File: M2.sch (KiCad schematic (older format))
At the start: 3 parts

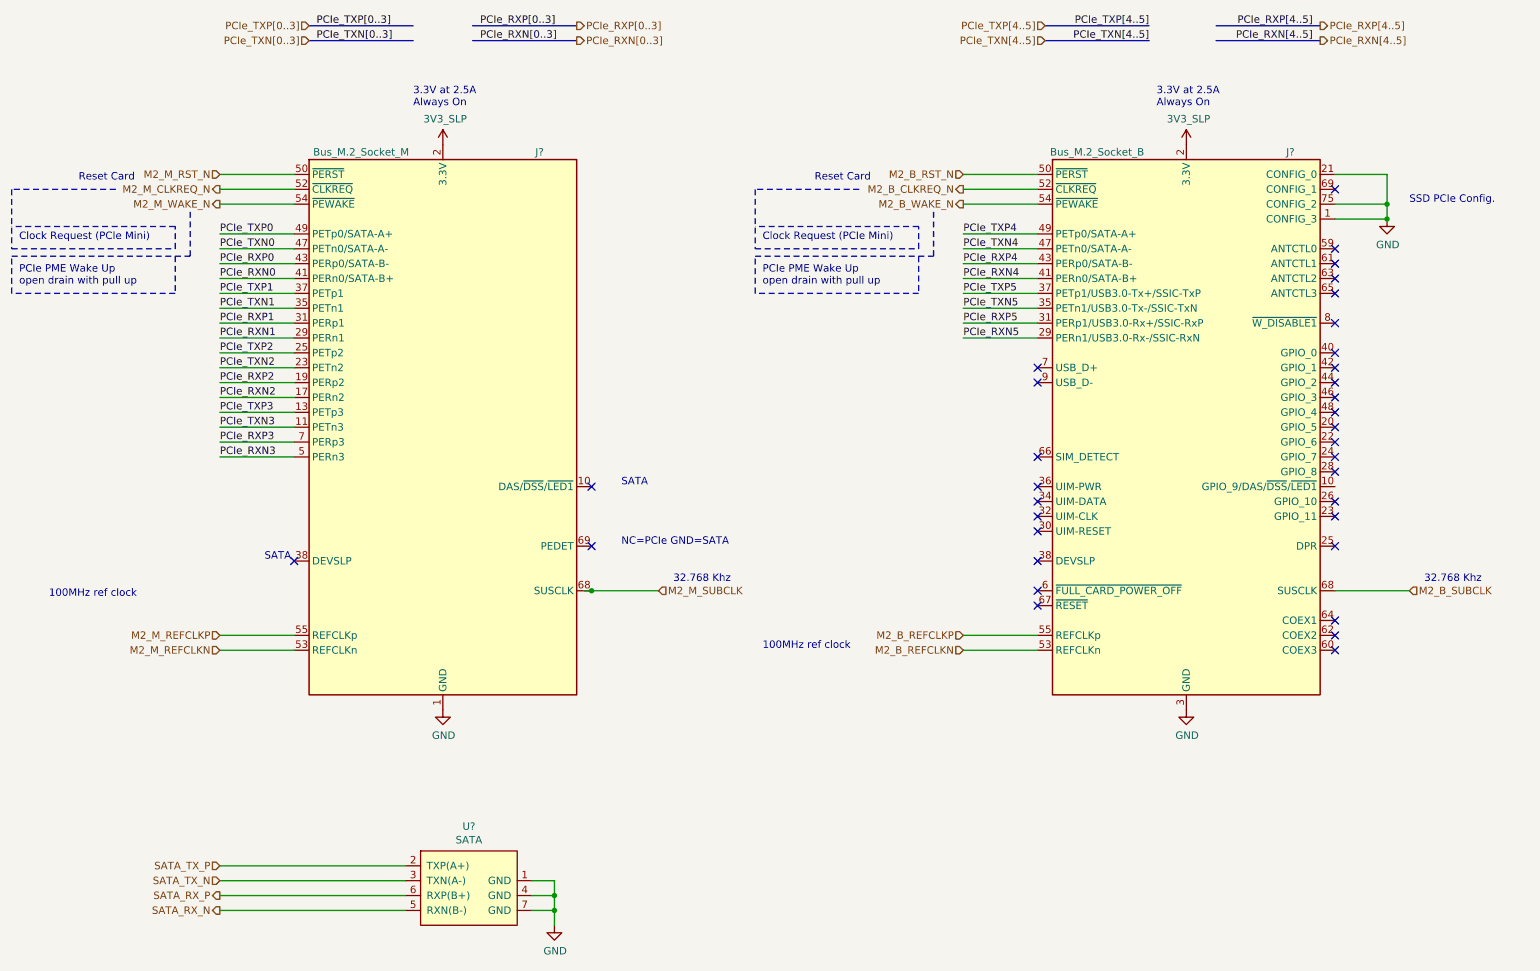
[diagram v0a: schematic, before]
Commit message: Add pull-up for PERST signals
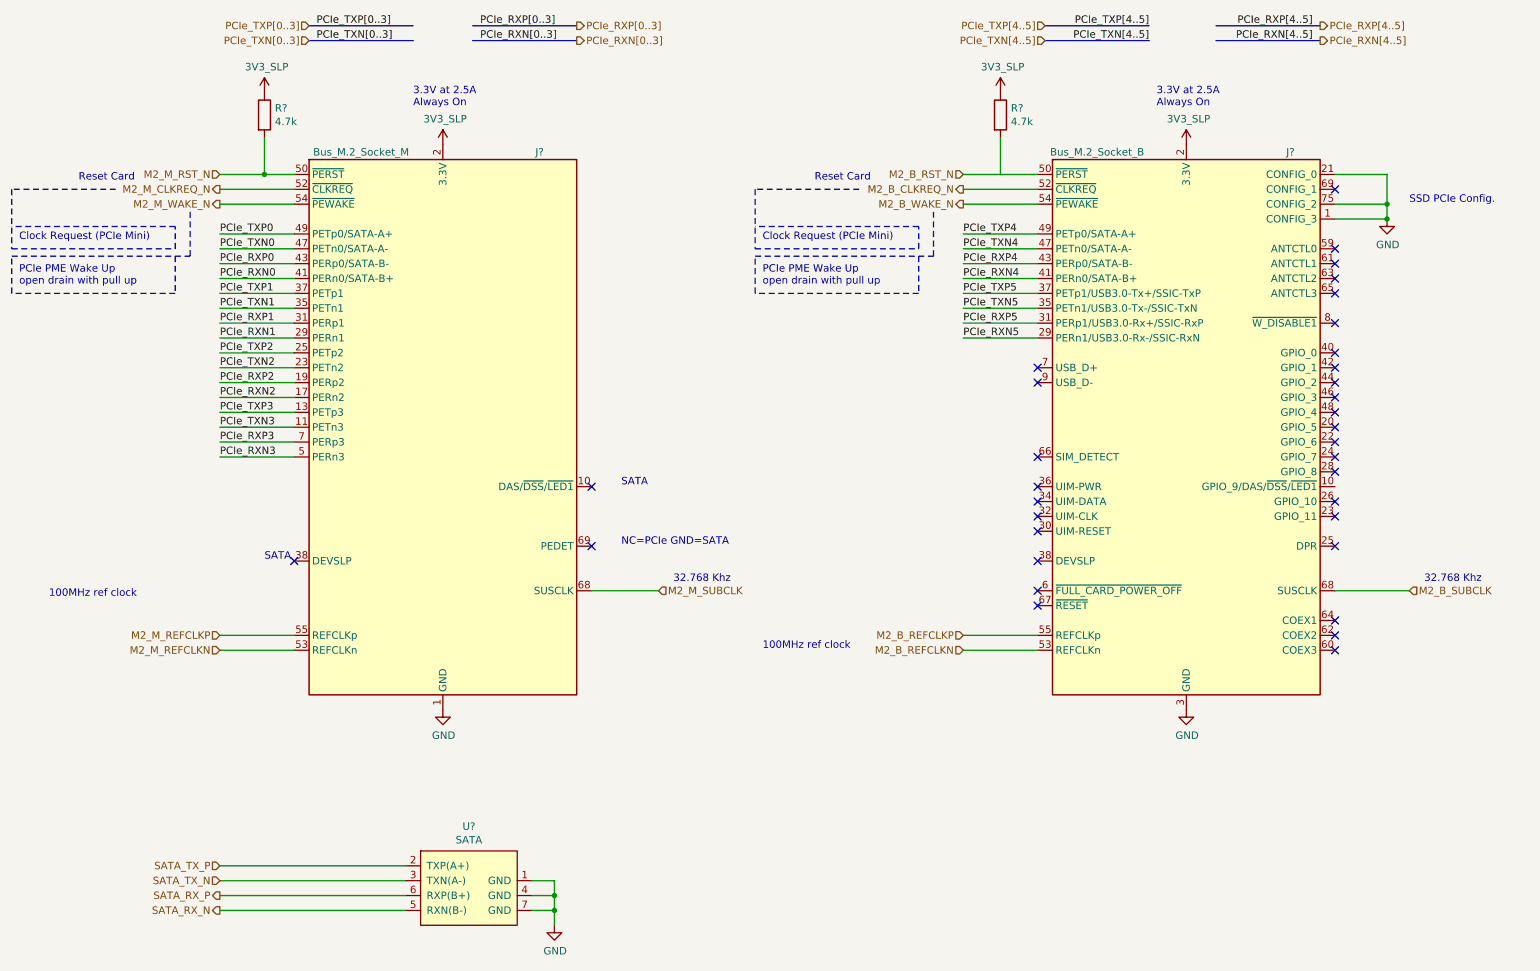
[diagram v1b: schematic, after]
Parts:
- added R? (x2): 4.7k, symbol Device:R
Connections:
- net 3V3_SLP: now also R?.1, R?.1
- net M2_M_RST_N: now also R?.2
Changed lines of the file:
@@
 $Descr A4 11693 8268
 encoding utf-8
-Sheet 18 28
+Sheet 17 28
 Title "DJANGO"
 Date "2020-12-06"
@@
 Wire Bus Line
 	3650 850  4350 850
-Wire Wire Line
-	2450 2250 1950 2250
-Wire Wire Line
-	2450 2350 1950 2350
-Wire Wire Line
-	2450 2450 1950 2450
-Wire Wire Line
-	2450 2550 1950 2550
-Wire Wire Line
-	2450 2650 1950 2650
-Wire Wire Line
-	2450 2750 1950 2750
-Wire Wire Line
-	2450 2850 1950 2850
-Wire Wire Line
-	2450 3050 1950 3050
-Wire Wire Line
-	2450 3150 1950 3150
-Wire Wire Line
-	2450 3250 1950 3250
-Wire Wire Line
-	2450 3350 1950 3350
-Wire Wire Line
-	2450 3450 1950 3450
-Wire Wire Line
-	2450 3550 1950 3550
-Wire Wire Line
-	2450 3650 1950 3650
 Wire Wire Line
 	2450 3750 1950 3750
@@
 	1    0    0    -1
 $EndComp
-Wire Wire Line
-	2450 2950 1950 2950
-Wire Wire Line
-	2450 1850 1950 1850
 Text HLabel 1950 1850 0    50   Input ~ 0
 M2_M_RST_N
@@
 NoConn ~ 2450 4450
 NoConn ~ 4450 3950
-Wire Wire Line
-	2450 1950 1950 1950
 Text HLabel 1950 1950 0    50   Output ~ 0
 M2_M_CLKREQ_N
@@
 	6650 2350 6650 2200
 Wire Wire Line
-	2450 4950 1950 4950
-Wire Wire Line
 	2450 5050 1950 5050
 Text HLabel 1950 4950 0    50   Input ~ 0
@@
 Text HLabel 6950 5050 0    50   Input ~ 0
 M2_B_REFCLKN
-Wire Wire Line
-	4400 4650 4450 4650
 Text HLabel 4900 4650 2    50   Input ~ 0
 M2_M_SUBCLK
@@
 	1    0    0    -1
 $EndComp
-Connection ~ 4450 4650
 Wire Wire Line
 	4450 4650 4900 4650
@@
 Wire Wire Line
 	3200 6800 1950 6800
+$Comp
+L ppc_scm:3V3_SLP #PWR?
+U 1 1 608080F8
+P 2250 1300
+F 0 "#PWR?" H 2250 1150 50  0001 C CNN
+F 1 "3V3_SLP" H 2265 1473 50  0000 C CNN
+F 2 "" H 2250 1300 50  0001 C CNN
+F 3 "" H 2250 1300 50  0001 C CNN
+	1    2250 1300
+	1    0    0    -1
+$EndComp
+$Comp
+L Device:R R?
+U 1 1 6080963A
+P 2250 1450
+F 0 "R?" H 2320 1496 50  0000 L CNN
+F 1 "4.7k" H 2320 1405 50  0000 L CNN
+F 2 "" V 2180 1450 50  0001 C CNN
+F 3 "~" H 2250 1450 50  0001 C CNN
+	1    2250 1450
+	1    0    0    -1
+$EndComp
+Wire Wire Line
+	2250 1600 2250 1850
+Connection ~ 2250 1850
+Wire Wire Line
+	2250 1850 1950 1850
+$Comp
+L ppc_scm:3V3_SLP #PWR?
+U 1 1 6080DE01
+P 7200 1300
+F 0 "#PWR?" H 7200 1150 50  0001 C CNN
+F 1 "3V3_SLP" H 7215 1473 50  0000 C CNN
+F 2 "" H 7200 1300 50  0001 C CNN
+F 3 "" H 7200 1300 50  0001 C CNN
+	1    7200 1300
+	1    0    0    -1
+$EndComp
+$Comp
+L Device:R R?
+U 1 1 6080DE07
+P 7200 1450
+F 0 "R?" H 7270 1496 50  0000 L CNN
+F 1 "4.7k" H 7270 1405 50  0000 L CNN
+F 2 "" V 7130 1450 50  0001 C CNN
+F 3 "~" H 7200 1450 50  0001 C CNN
+	1    7200 1450
+	1    0    0    -1
+$EndComp
+Wire Wire Line
+	7200 1600 7200 1850
+Wire Wire Line
+	1950 2250 2450 2250
+Wire Wire Line
+	1950 2350 2450 2350
+Wire Wire Line
+	1950 2450 2450 2450
+Wire Wire Line
+	1950 2550 2450 2550
+Wire Wire Line
+	1950 2650 2450 2650
+Wire Wire Line
+	1950 2750 2450 2750
+Wire Wire Line
+	1950 2850 2450 2850
+Wire Wire Line
+	1950 3050 2450 3050
+Wire Wire Line
+	1950 3150 2450 3150
+Wire Wire Line
+	1950 3250 2450 3250
+Wire Wire Line
+	1950 3350 2450 3350
+Wire Wire Line
+	1950 3450 2450 3450
+Wire Wire Line
+	1950 3550 2450 3550
+Wire Wire Line
+	1950 3650 2450 3650
+Wire Wire Line
+	1950 2950 2450 2950
+Wire Wire Line
+	2250 1850 2450 1850
+Wire Wire Line
+	1950 1950 2450 1950
+Wire Wire Line
+	1950 4950 2450 4950
 $EndSCHEMATC
